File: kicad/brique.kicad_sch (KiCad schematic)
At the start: 51 parts, among them J1 Conn_01x07, J2 USB_B_Micro, J3 Speaker Pads, J4 Battery Connection Pads, J6 BM03B-SRSS-TB, J7 BM03B-SRSS-TB, M1 Vibration, Q1 BC847, SW2 BOOT, U1 W25Q128JVS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

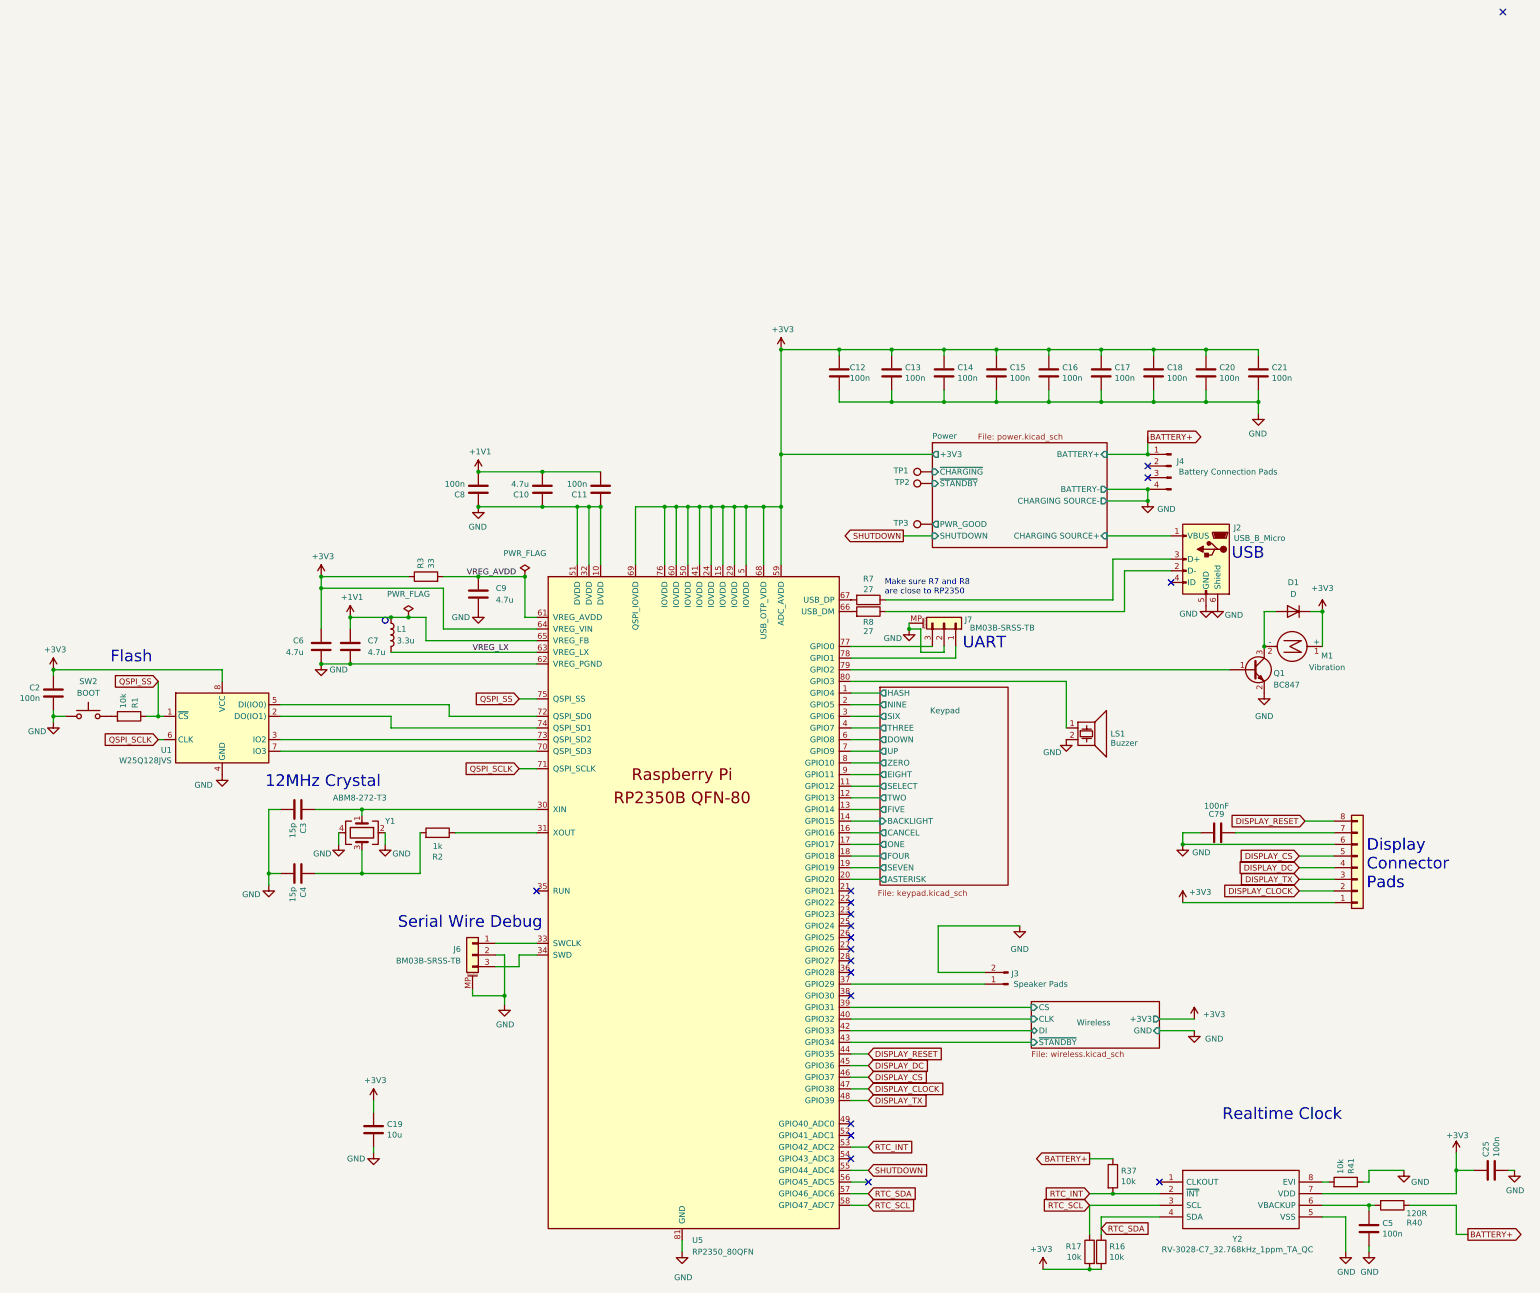
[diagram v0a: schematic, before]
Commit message: snake, fix pcb errors, update menu
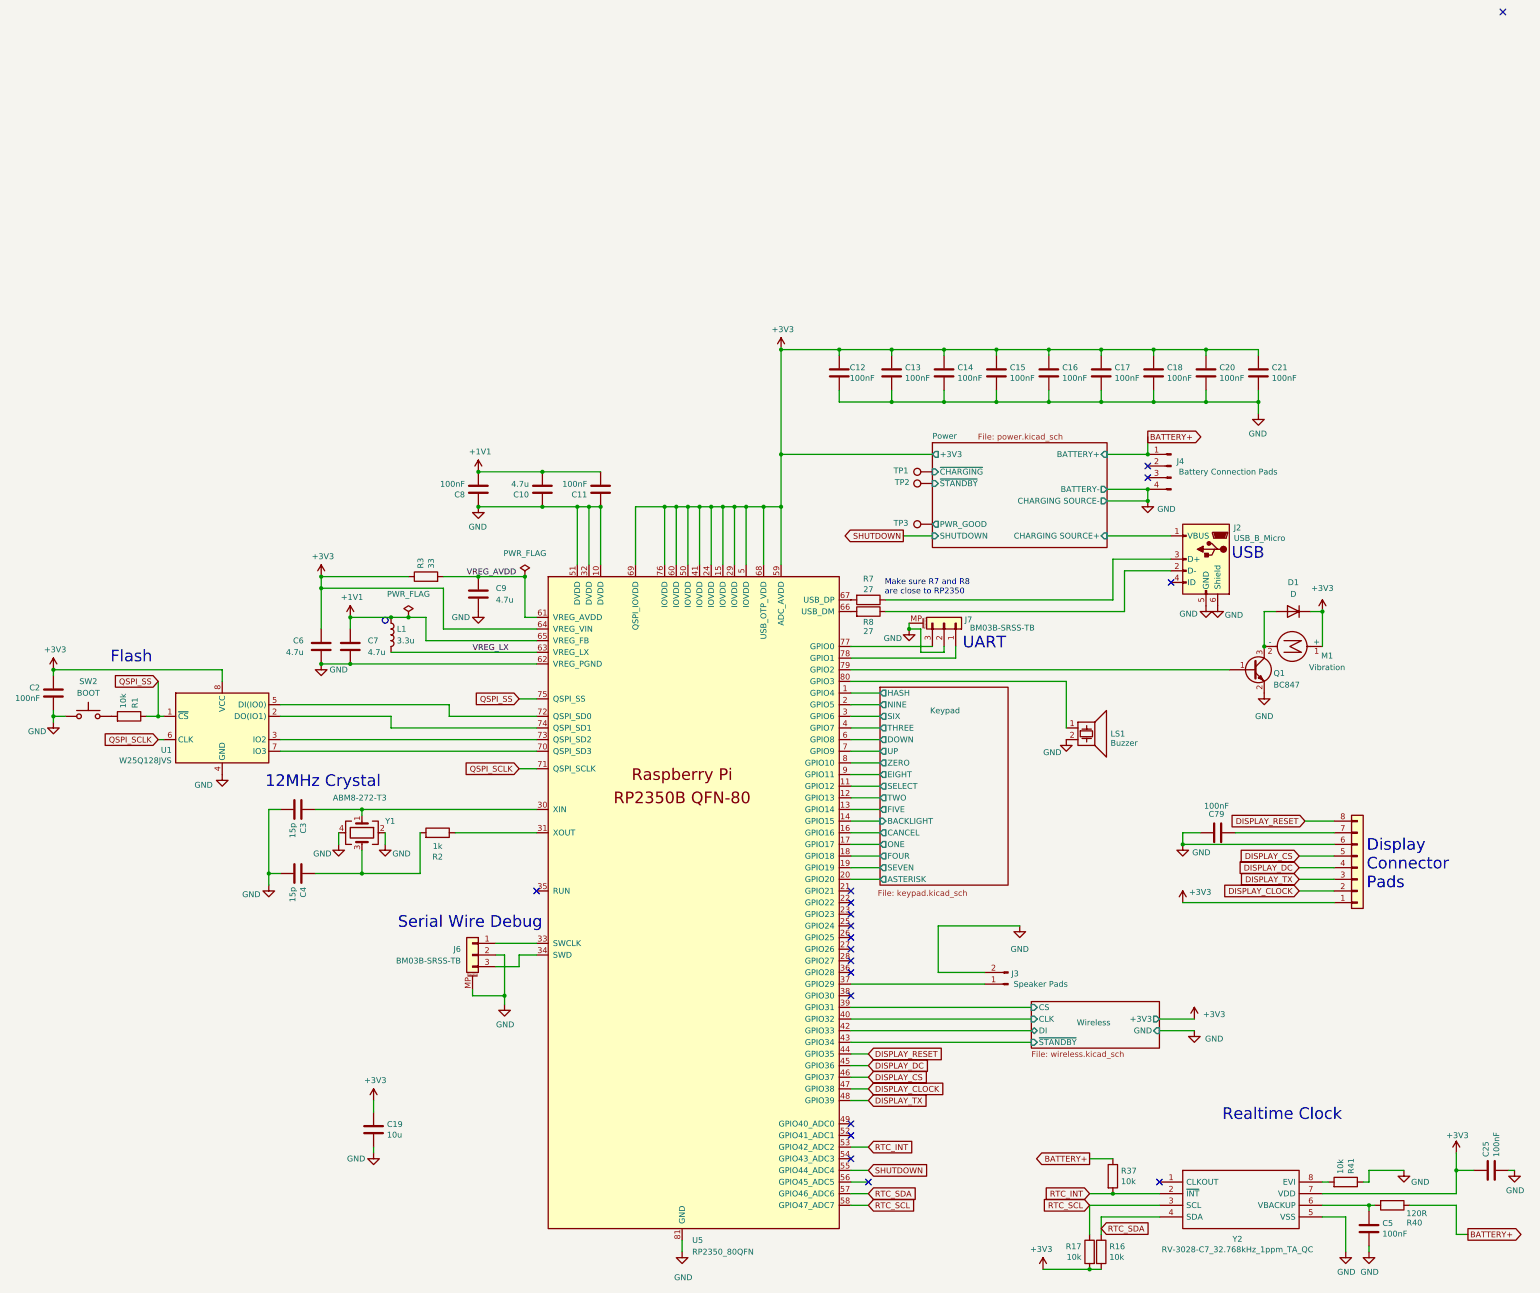
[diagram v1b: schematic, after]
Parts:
- C11, C12, C13, C14, C15, C16, C17, C18, C2, C20, C21, C25, C5, C8: value 100n -> 100nF
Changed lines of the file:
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@@
 			)
 		)
-		(property "Value" "100n"
+		(property "Value" "100nF"
 			(at 242.316 44.323 0)
 			(effects
@@
 			)
 		)
-		(property "Value" "100n"
+		(property "Value" "100nF"
 			(at 300.101 44.323 0)
 			(effects
@@
 			)
 		)
-		(property "Value" "100n"
+		(property "Value" "100nF"
 			(at 265.811 44.323 0)
 			(effects
@@
 			)
 		)
-		(property "Value" "100n"
+		(property "Value" "100nF"
 			(at 383.413 214.249 0)
 			(effects
@@
 			)
 		)
-		(property "Value" "100n"
+		(property "Value" "100nF"
 			(at 311.531 44.323 0)
 			(effects
@@
 			)
 		)
-		(property "Value" "100n"
+		(property "Value" "100nF"
 			(at 65.659 114.173 0)
 			(effects
@@
 			)
 		)
-		(property "Value" "100n"
+		(property "Value" "100nF"
 			(at 288.671 44.323 0)
 			(effects
@@
 			)
 		)
-		(property "Value" "100n"
+		(property "Value" "100nF"
 			(at 277.241 44.323 0)
 			(effects
@@
 			)
 		)
-		(property "Value" "100n"
+		(property "Value" "100nF"
 			(at 358.521 231.013 0)
 			(effects
@@
 			)
 		)
-		(property "Value" "100n"
+		(property "Value" "100nF"
 			(at 322.961 44.323 0)
 			(effects
@@
 			)
 		)
-		(property "Value" "100n"
+		(property "Value" "100nF"
 			(at 185.039 67.437 0)
 			(effects
@@
 			)
 		)
-		(property "Value" "100n"
+		(property "Value" "100nF"
 			(at 254.381 44.323 0)
 			(effects
@@
 			)
 		)
-		(property "Value" "100n"
+		(property "Value" "100nF"
 			(at 158.369 67.437 0)
 			(effects
@@
 			)
 		)
-		(property "Value" "100n"
+		(property "Value" "100nF"
 			(at 334.391 44.323 0)
 			(effects
